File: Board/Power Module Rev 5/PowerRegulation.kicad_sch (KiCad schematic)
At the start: 8 parts, among them U14 TPS2116DRLR, U15 NCP167BMX330TBG

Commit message: Board Progress
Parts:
- added C44, C47: 100nF, Capacitor_SMD:C_0603_1608Metric_Pad1.08x0.95mm_HandSolder, symbol Device:C_Small
- added C45: 4.7uF, Capacitor_SMD:C_1210_3225Metric_Pad1.33x2.70mm_HandSolder, symbol Device:C_Small
- added C46: 39pF, Capacitor_SMD:C_0603_1608Metric_Pad1.08x0.95mm_HandSolder, symbol Device:C_Small
- added C48: 47uF, Capacitor_SMD:C_1210_3225Metric_Pad1.33x2.70mm_HandSolder, symbol Device:C_Small
- added L1: 39uH, Inductor_SMD:L_Wuerth_WE-PD-Typ-LS, symbol Device:L_Small
- added R62: 100k, Resistor_SMD:R_0603_1608Metric_Pad0.98x0.95mm_HandSolder, symbol Device:R_Small
- added R63: 64.9k, Resistor_SMD:R_0603_1608Metric_Pad0.98x0.95mm_HandSolder, symbol Device:R_Small
- added R64: 40.2k, Resistor_SMD:R_0603_1608Metric_Pad0.98x0.95mm_HandSolder, symbol Device:R_Small
- added R65: 10k, Resistor_SMD:R_0603_1608Metric_Pad0.98x0.95mm_HandSolder, symbol Device:R_Small
- added U16: PLMR38010FSQDDARQ1, MyKiCadLibraries:HSOP8_DDA_TEX, symbol MyLibrary:PLMR38010FSQDDARQ1
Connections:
- net EPAD: now also C44.2, C45.2, C48.2, R63.2, R65.1, U16.1 (gnd), U16.9 (EPAD)
- net Regulated 5V: now also C46.1, C48.1, L1.2, R62.2, R64.2
- new net: R62.1, U16.6 (pg)
- new net: R63.1, U16.4 (rt/sync)
- new net: C46.2, R64.1, R65.2, U16.5 (fb)
- new net: C47.1, U16.7 (boot)
- new net: C47.2, L1.1, U16.8 (sw)
- new net Ignition: C44.1, C45.1, U16.2 (en), U16.3 (vin)
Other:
- moved on the sheet: C42, C43, R58, R59, R60, R61, U14, U15

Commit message: Board Update
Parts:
- removed R61: 10K, Resistor_SMD:R_0603_1608Metric_Pad0.98x0.95mm_HandSolder, symbol Device:R_Small
- removed U15: NCP167BMX330TBG, Package_DFN_QFN:OnSemi_XDFN4-1EP_1.0x1.0mm_EP0.52x0.52mm, symbol MyLibrary:NCP167BMX330TBG
- added U1: AP2112K-3.3, Package_TO_SOT_SMD:SOT-23-5, symbol Regulator_Linear:AP2112K-3.3
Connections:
- net +3.3V: now also U1.5 (VOUT)
- net +5V: now also U1.1 (VIN), U1.3 (EN)
- net EPAD renamed GND
- net GND: now also U1.2 (GND)
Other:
- moved on the sheet: C42, C43

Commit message: Update config and renames on schematic
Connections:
- net Power Switch Status renamed PowerSwitchStatus
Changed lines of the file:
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@@
     )
   )
-  (global_label "Power Switch Status" (shape input) (at 128.27 121.92 0) (fields_autoplaced)
+  (global_label "PowerSwitchStatus" (shape input) (at 128.27 121.92 0) (fields_autoplaced)
     (effects (font (size 1.27 1.27)) (justify left))
-    (property "Intersheetrefs" "${INTERSHEET_REFS}" (at 150.4192 121.92 0)
+    (property "Intersheetrefs" "${INTERSHEET_REFS}" (at 148.8952 121.92 0)
       (effects (font (size 1.27 1.27)) (justify left) hide)
     )

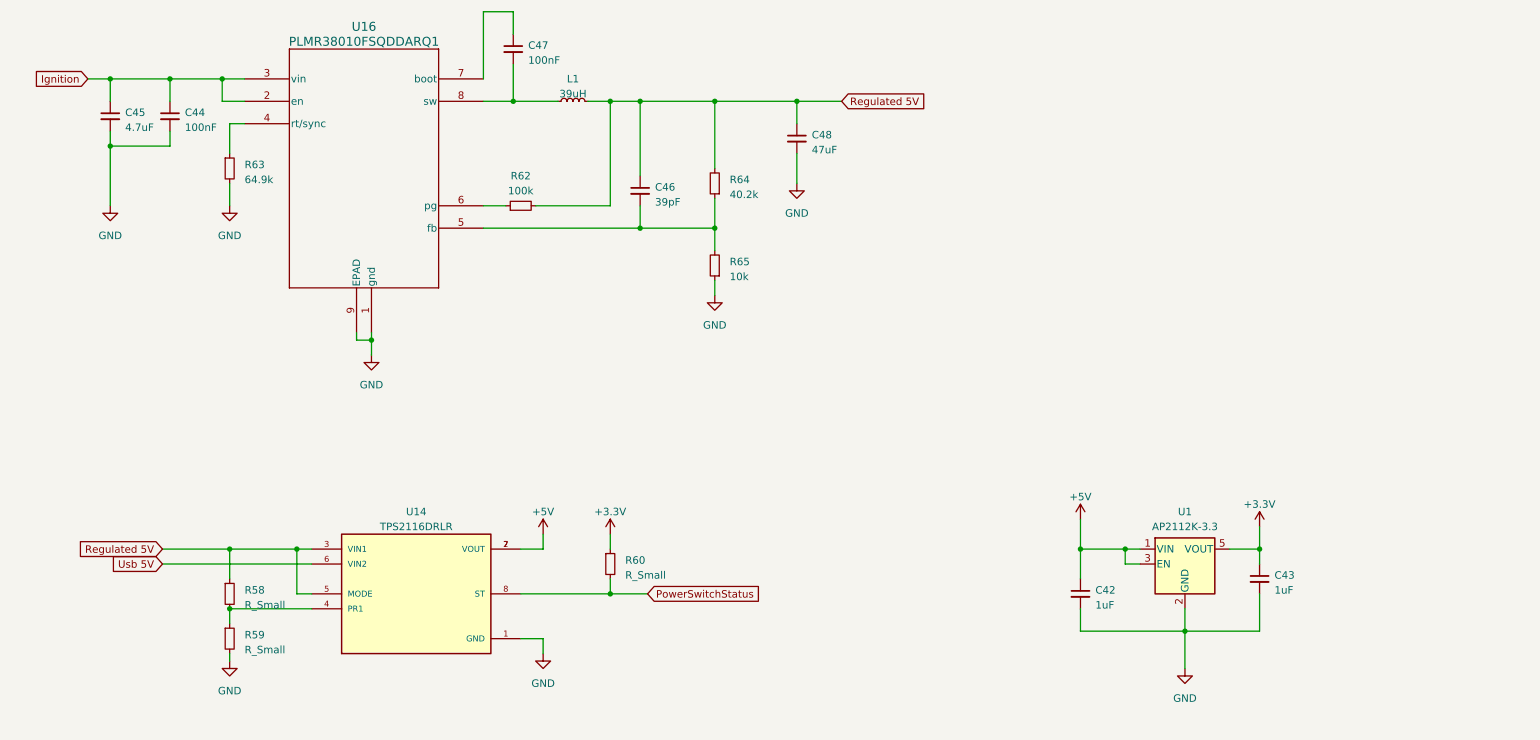
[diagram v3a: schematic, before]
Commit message: Board - changed regulator
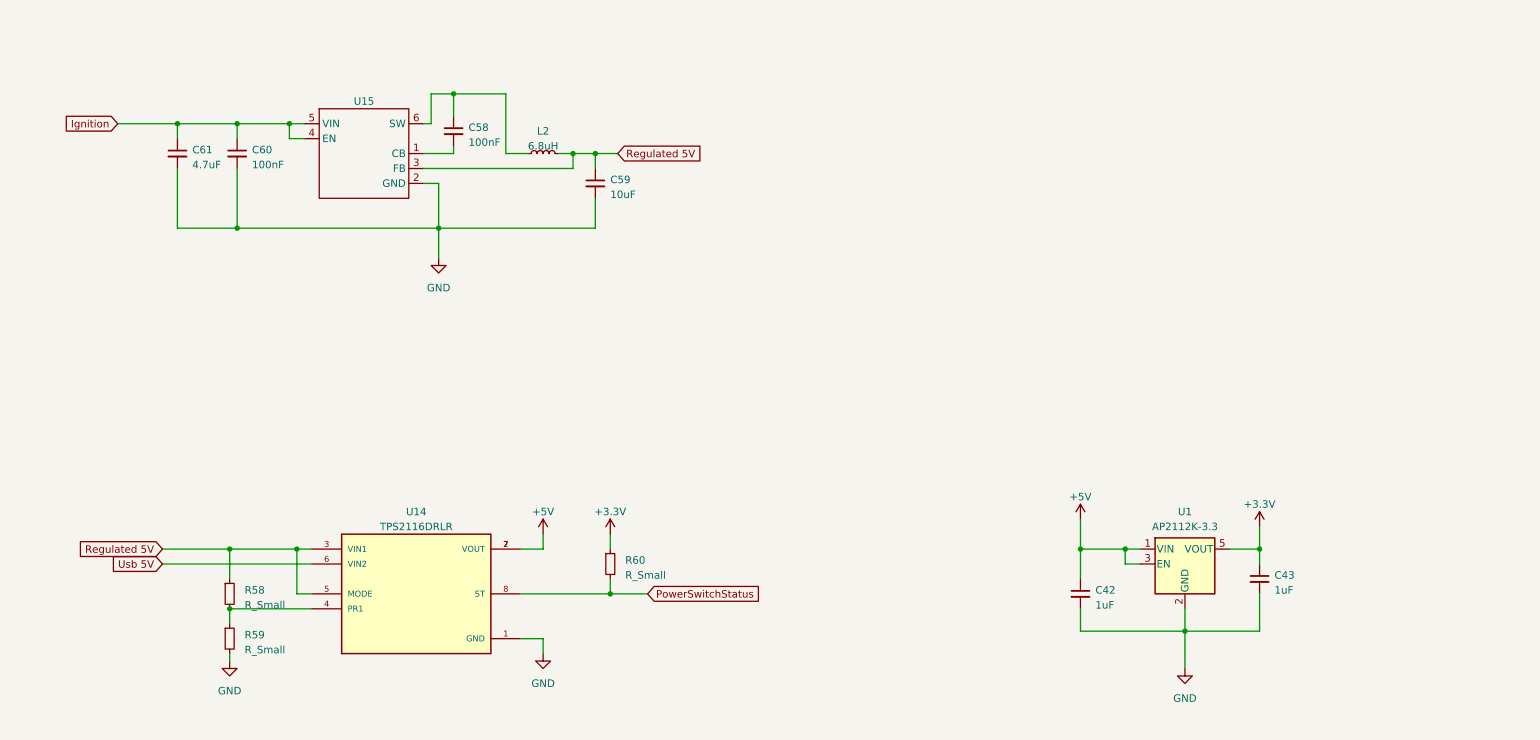
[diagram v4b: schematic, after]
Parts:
- removed C44, C47: 100nF, Capacitor_SMD:C_0603_1608Metric_Pad1.08x0.95mm_HandSolder, symbol Device:C_Small
- removed C45: 4.7uF, Capacitor_SMD:C_1210_3225Metric_Pad1.33x2.70mm_HandSolder, symbol Device:C_Small
- removed C46: 39pF, Capacitor_SMD:C_0603_1608Metric_Pad1.08x0.95mm_HandSolder, symbol Device:C_Small
- removed C48: 47uF, Capacitor_SMD:C_1210_3225Metric_Pad1.33x2.70mm_HandSolder, symbol Device:C_Small
- removed L1: 39uH, Inductor_SMD:L_Wuerth_WE-PD-Typ-LS, symbol Device:L_Small
- removed R62: 100k, Resistor_SMD:R_0603_1608Metric_Pad0.98x0.95mm_HandSolder, symbol Device:R_Small
- removed R63: 64.9k, Resistor_SMD:R_0603_1608Metric_Pad0.98x0.95mm_HandSolder, symbol Device:R_Small
- removed R64: 40.2k, Resistor_SMD:R_0603_1608Metric_Pad0.98x0.95mm_HandSolder, symbol Device:R_Small
- removed R65: 10k, Resistor_SMD:R_0603_1608Metric_Pad0.98x0.95mm_HandSolder, symbol Device:R_Small
- removed U16: PLMR38010FSQDDARQ1, MyKiCadLibraries:HSOP8_DDA_TEX, symbol MyLibrary:PLMR38010FSQDDARQ1
- added C58: 100nF, Capacitor_SMD:C_0603_1608Metric_Pad1.08x0.95mm_HandSolder, symbol Device:C_Small
- added C59: 10uF, Capacitor_SMD:C_0805_2012Metric_Pad1.18x1.45mm_HandSolder, symbol Device:C_Small
- added C60: 100nF, Capacitor_SMD:C_0805_2012Metric_Pad1.18x1.45mm_HandSolder, symbol Device:C_Small
- added C61: 4.7uF, Capacitor_SMD:C_0805_2012Metric_Pad1.18x1.45mm_HandSolder, symbol Device:C_Small
- added L2: 6.8uH, Inductor_SMD_Wurth:L_Wurth_WE-LQSH-4020, symbol Device:L_Small
- added U15: ~, Package_TO_SOT_SMD:SOT-23-6_Handsoldering, symbol MyLibrary:LMR50410Y5FQDBVRQ1_
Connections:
- net GND: now also C59.2, C60.2, C61.2, U15.2 (GND)
- net Ignition: now also C60.1, C61.1, U15.4 (EN), U15.5 (VIN)
- net Regulated 5V: now also C59.1, L2.2, U15.3 (FB)
- new net: C58.1, L2.1, U15.6 (SW)
- new net: C58.2, U15.1 (CB)

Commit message: Board Update and Gerbers
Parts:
- C58, C60: value 100nF -> 0.1uF
- R58, R59, R60: value R_Small -> 10K
- U15: value ~ -> LMR50410Y5FQDBVRQ1
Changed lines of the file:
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@@
       (effects (font (size 1.27 1.27)) (justify left))
     )
-    (property "Value" "100nF" (at 60.96 48.9013 0)
+    (property "Value" "0.1uF" (at 60.96 48.9013 0)
       (effects (font (size 1.27 1.27)) (justify left))
     )
@@
       (effects (font (size 1.27 1.27)) (justify left))
     )
-    (property "Value" "R_Small" (at 59.69 123.825 0)
+    (property "Value" "10K" (at 59.69 123.825 0)
       (effects (font (size 1.27 1.27)) (justify left))
     )
@@
       (effects (font (size 1.27 1.27)))
     )
-    (property "Value" "~" (at 80.01 45.72 0)
-      (effects (font (size 1.27 1.27)))
+    (property "Value" "LMR50410Y5FQDBVRQ1" (at 80.01 45.72 0)
+      (effects (font (size 1.27 1.27)) hide)
     )
     (property "Footprint" "Package_TO_SOT_SMD:SOT-23-6_Handsoldering" (at 80.01 45.72 0)
@@
       (effects (font (size 1.27 1.27)) (justify left))
     )
-    (property "Value" "R_Small" (at 59.69 131.445 0)
+    (property "Value" "10K" (at 59.69 131.445 0)
       (effects (font (size 1.27 1.27)) (justify left))
     )
@@
       (effects (font (size 1.27 1.27)) (justify left))
     )
-    (property "Value" "R_Small" (at 124.46 118.745 0)
+    (property "Value" "10K" (at 124.46 118.745 0)
       (effects (font (size 1.27 1.27)) (justify left))
     )
@@
       (effects (font (size 1.27 1.27)) (justify left))
     )
-    (property "Value" "100nF" (at 97.79 45.0913 0)
-      (effects (font (size 1.27 1.27)) (justify left))
-    )
+    (property "Value" "0.1uF" (at 97.79 45.0913 0)
+      (effects (font (size 1.27 1.27)) (justify left))
+    )
